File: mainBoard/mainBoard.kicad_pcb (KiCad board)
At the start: 4 copper layers, 50 x 60 mm, 43 parts, among them J1 Conn_01x04, J10 Conn_02x07_Odd_Even, J2 Conn_01x04, J4 Conn_01x01, J5 Conn_01x01, J6 Conn_01x07, J7 Conn_01x07, J8 Conn_01x02, J9 Conn_01x08, U1 MAX15062A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

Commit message: Popisky
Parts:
- renumbered J4 to M1, J5 to M2
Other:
- board text added: "+"
- board text added: "-"
- board text added: "BAT_SENS"
- board text added: "ENC_POT"
- board text added: "G"
- board text added: "M1"
- board text added: "M2"
- board text added: "NRST"
- board text added: "PROUD"
- board text added: "R"
- board text added: "RST"
- board text added: "RX"
- board text added: "SWCLK"
- board text added: "SWDIO"
- board text added: "T"
- board text added: "TX"
- board text added: "VREF"

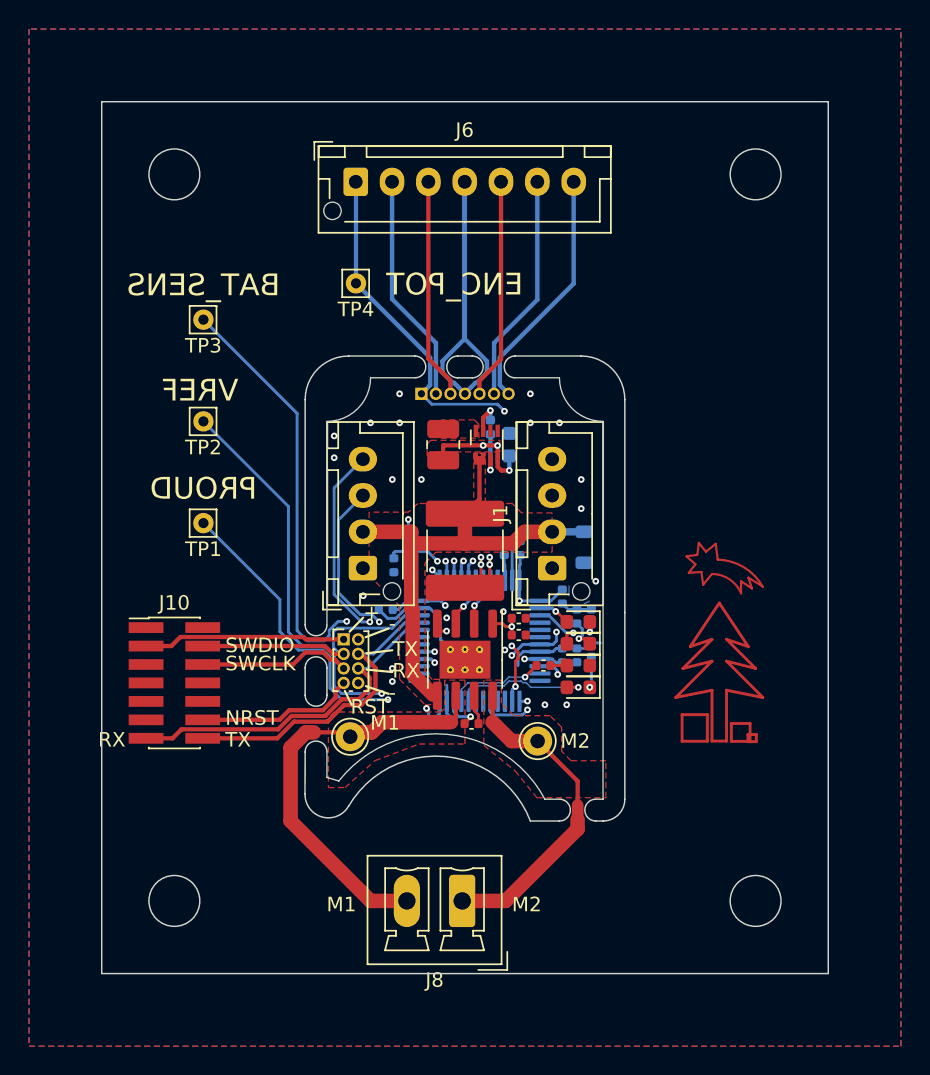
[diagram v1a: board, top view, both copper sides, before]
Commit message: Zvetšení test pointů
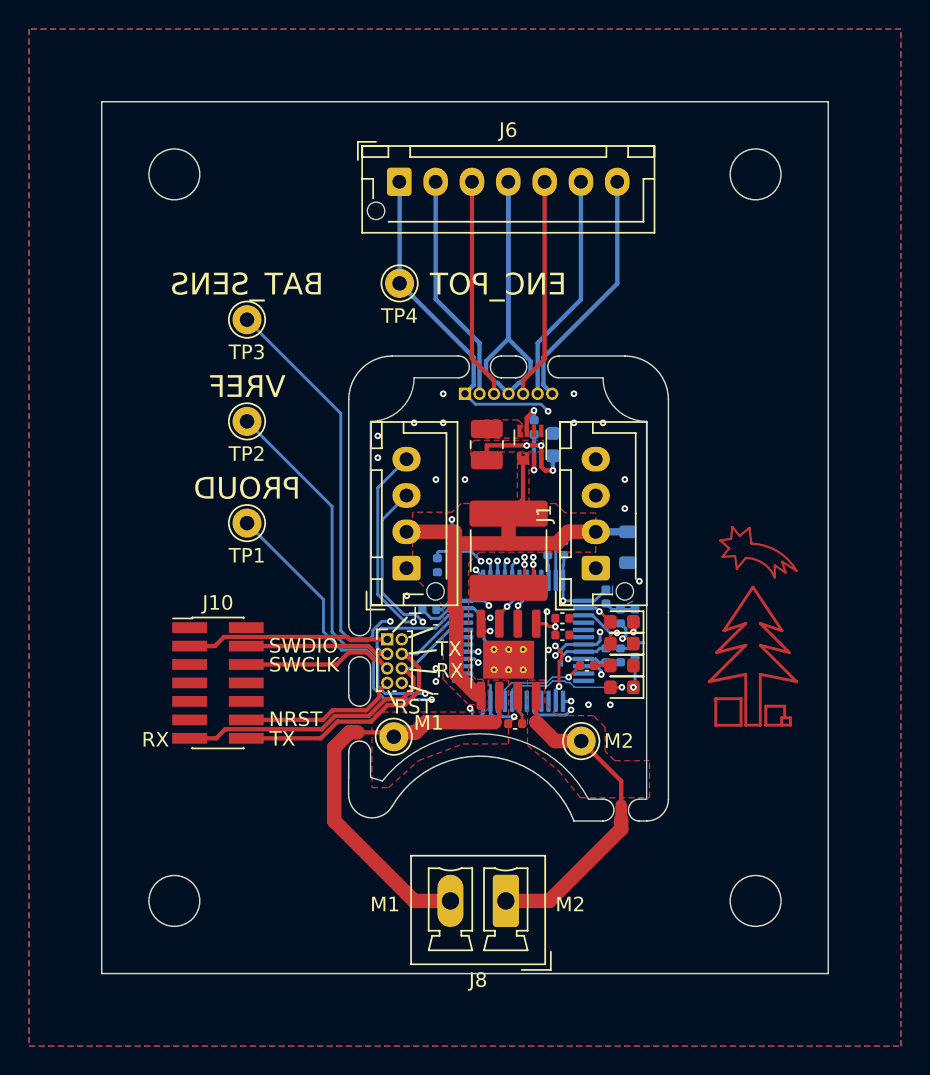
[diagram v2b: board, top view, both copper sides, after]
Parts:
- TP1, TP2, TP3, TP4: footprint Connector_Pin:Pin_D0.7mm_L6.5mm_W1.8mm_FlatFork -> Connector_Pin:Pin_D1.0mm_L10.0mm
- moved C1 3.00 mm to (148.1, 96.9)
- moved C10 3.00 mm to (159.7, 103.1)
- moved C11 3.00 mm to (153.4, 107.8)
- moved C12 3.00 mm to (160.7, 103.1)
- moved C13 3.00 mm to (155.7, 95.7)
- moved C14 3.00 mm to (153.0, 95.9)
- moved C15 3.00 mm to (156.7, 101.7)
- moved C2 3.00 mm to (161.2, 95.7)
- moved C3 3.00 mm to (154.8, 87.4)
- moved C4 3.00 mm to (156.1, 88.6)
- moved C5 3.00 mm to (149.6, 107.8)
- moved C6 3.00 mm to (147.6, 100.0)
- moved C7 3.00 mm to (159.7, 99.0)
- moved C8 3.00 mm to (151.5, 107.8)
- moved C9 3.00 mm to (156.8, 95.7)
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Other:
- outline, holes or cut-outs redrawn

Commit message: Hrádky s poligony
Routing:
- net GND: track 54.4 -> 76.8 mm
- net VCC: track 35.2 -> 36.2 mm
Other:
- board text added: "CLK"
- board text added: "E.TYP"
- board text added: "MISO"
- board text added: "MOSI"
- board text added: "POT"

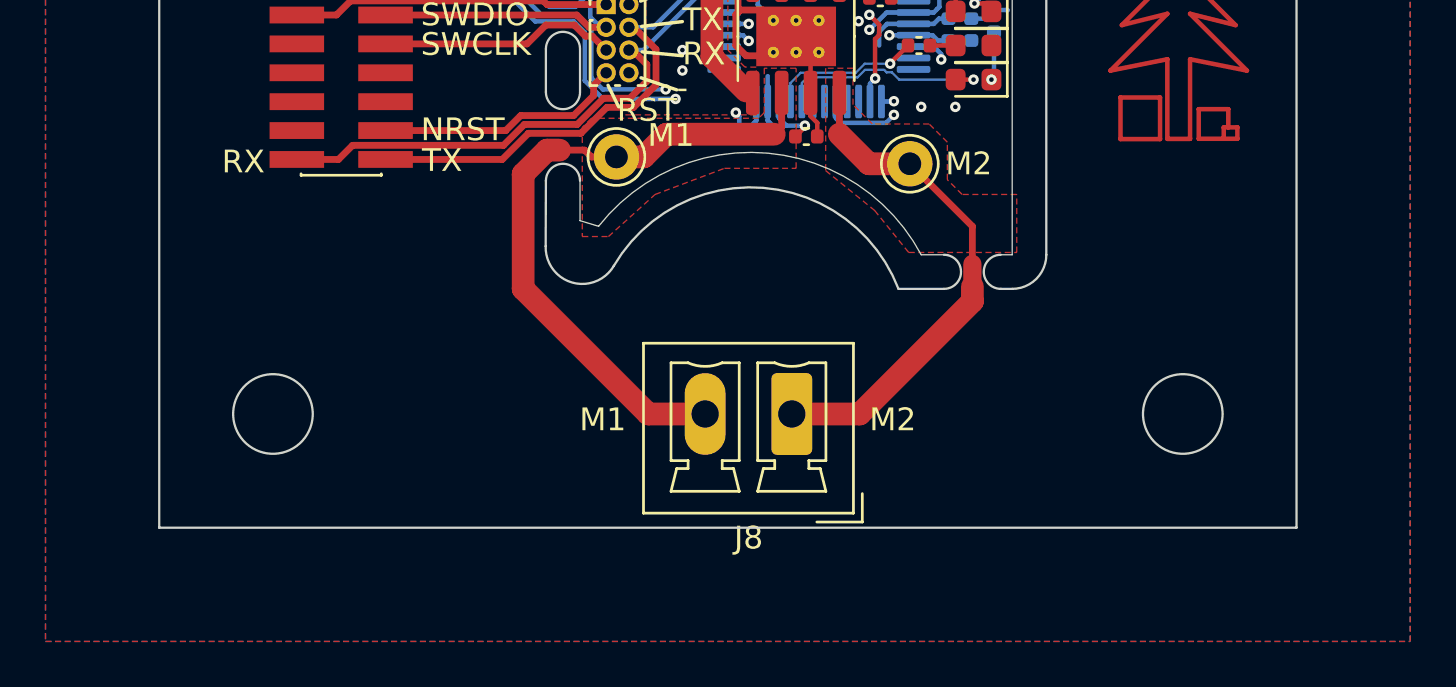
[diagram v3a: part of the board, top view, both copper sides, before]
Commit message: JST-XH na externí motorový konektor
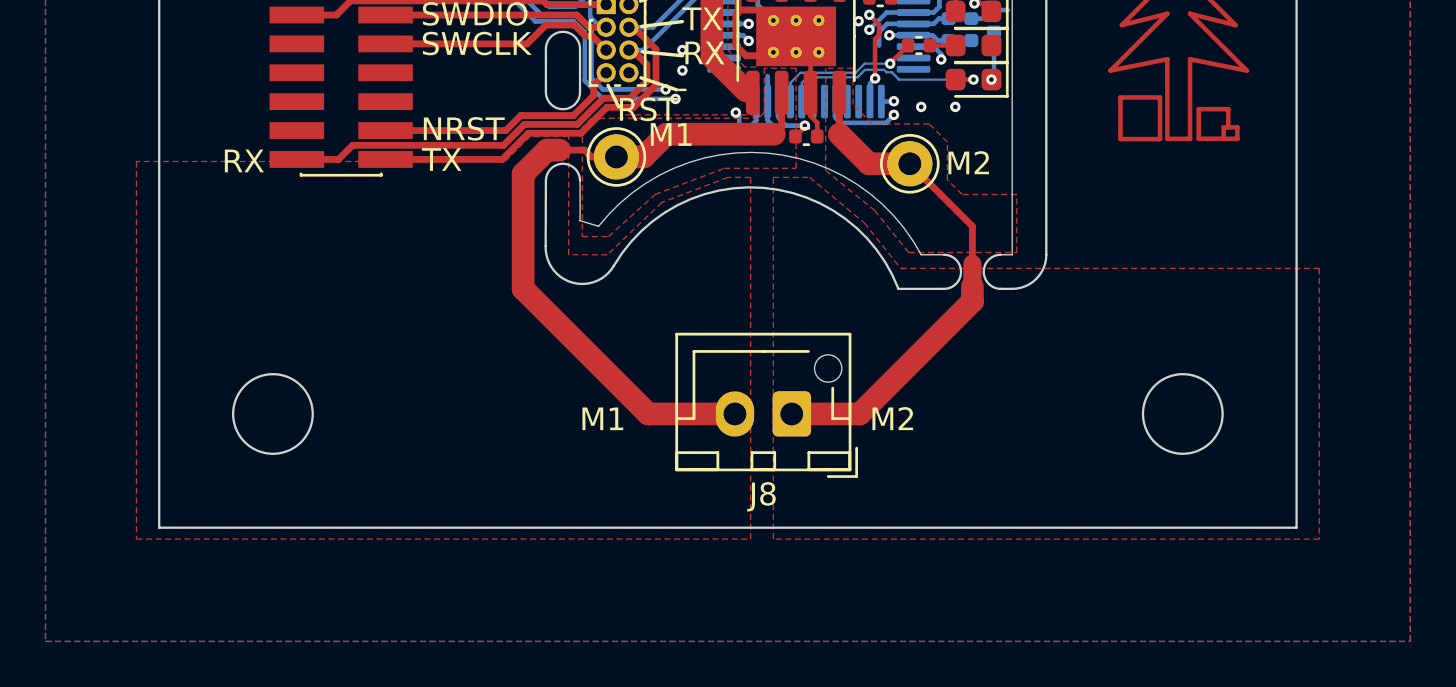
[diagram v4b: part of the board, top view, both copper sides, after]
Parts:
- J8: footprint Connector_Phoenix_MC:PhoenixContact_MCV_1,5_2-G-3.81_1x02_P3.81mm_Vertical -> Connector_JST:JST_XH_B2B-XH-AM_1x02_P2.50mm_Vertical
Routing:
- net Net-(J8-Pin_2): track 29.3 -> 30.6 mm

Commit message: Moc kondíků
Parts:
- added C16: 2u2, Capacitor_SMD:C_0805_2012Metric, F.Cu at (153.0, 92.5)
- added C17: 2u2, Capacitor_SMD:C_0805_2012Metric, F.Cu at (155.1, 92.5)
- added C18: 2u2, Capacitor_SMD:C_0805_2012Metric, F.Cu at (150.9, 96.0)
- added C19: 2u2, Capacitor_SMD:C_0805_2012Metric, F.Cu at (153.0, 96.0)
- added C20: 2u2, Capacitor_SMD:C_0805_2012Metric, F.Cu at (155.1, 96.0)
- added C22: 2u2, Capacitor_SMD:C_0805_2012Metric, F.Cu at (148.5, 102.3)
- added C23: 2u2, Capacitor_SMD:C_0805_2012Metric, F.Cu at (148.5, 104.2)
- added C24: 2u2, Capacitor_SMD:C_0805_2012Metric, F.Cu at (148.5, 106.2)
- added C25: 2u2, Capacitor_SMD:C_0805_2012Metric, F.Cu at (151.7, 98.7)
- added C26: 2u2, Capacitor_SMD:C_0805_2012Metric, B.Cu at (147.6, 106.5)
- added C27: 2u2, Capacitor_SMD:C_0805_2012Metric, B.Cu at (147.6, 102.9)
- added C28: 2u2, Capacitor_SMD:C_0805_2012Metric, B.Cu at (148.6, 95.9)
- added C29: 2u2, Capacitor_SMD:C_0805_2012Metric, B.Cu at (148.6, 92.3)
- added C30: 2u2, Capacitor_SMD:C_0805_2012Metric, B.Cu at (148.6, 88.5)
- added C31: 2u2, Capacitor_SMD:C_0805_2012Metric, B.Cu at (156.8, 92.6)
- added C32: 2u2, Capacitor_SMD:C_0805_2012Metric, B.Cu at (161.2, 92.1)
- added C33: 2u2, Capacitor_SMD:C_0805_2012Metric, B.Cu at (150.7, 88.5)
- added C34: 2u2, Capacitor_SMD:C_0805_2012Metric, B.Cu at (152.7, 88.5)
- C14: value 22u -> 2u2; footprint Capacitor_SMD:C_2220_5650Metric -> Capacitor_SMD:C_0805_2012Metric
- C2: value 1u -> 2u2; footprint Inductor_SMD:L_0805_2012Metric -> Capacitor_SMD:C_0805_2012Metric
- C3: footprint Inductor_SMD:L_0402_1005Metric -> Capacitor_SMD:C_0402_1005Metric
- moved C14 3.97 mm to (150.9, 92.5), turned to 90 degrees
- moved C1 3.94 mm to (145.6, 100.0), turned to 0 degrees
- moved R1 1.10 mm to (150.2, 95.0)
- moved R2 1.10 mm to (150.2, 96.9)
- moved J9 0.05 mm to (144.6, 102.0)
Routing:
- net VCC: track 36.2 -> 51.5 mm, vias 1 -> 4
- net GND: track 76.8 -> 82.6 mm
- net /CPU/UART.TX: track 29.8 -> 31.4 mm
- net /CPU/UART.RX: track 33.2 -> 34.3 mm
- net /CPU/ENC.ENC-TYP-DET: track 29.0 -> 29.8 mm
- net /CPU/ENC.MOSI: track 29.1 -> 28.4 mm
- net /CPU/RX-1: track 23.9 -> 24.6 mm, vias 0 -> 2
- net VDD: track 101.5 -> 102.2 mm
- net /CPU/TX-1: track 21.5 -> 20.9 mm
- net /CPU/SWCLK: track 23.5 -> 22.9 mm
- net /CPU/MEŘENÍ-NAPÁJENÍ: track 61.6 -> 61.0 mm
- added copper zone on In1.Cu, net GND
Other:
- board text removed: "RST"

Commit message: GNDDETECT
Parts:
- removed C34: 2u2, Capacitor_SMD:C_0805_2012Metric
- added C21: 2u2, Capacitor_SMD:C_0805_2012Metric, B.Cu at (152.7, 88.5)
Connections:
- J10 pad 11: unconnected-(J10-Pin_11-Pad11) -> GND

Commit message: 16x20
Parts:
- removed C19, C20, C21, C22, C23, C24, C25, C26, C27, C28, C29, C30, C31, C32, C33: 2u2, Capacitor_SMD:C_0805_2012Metric
- removed J9: Conn_01x08, Connector_PinHeader_1.00mm:PinHeader_2x04_P1.00mm_Vertical
- added J3: Conn_01x03, Connector_PinHeader_1.00mm:PinHeader_1x03_P1.00mm_Vertical, F.Cu at (145.6, 101.0)
- C10, C6, C7, C8, C9: footprint Capacitor_SMD:C_0402_1005Metric -> Capacitor_SMD:C_0201_0603Metric
- C11, R6: moved to B.Cu
- C14: value 2u2 -> 10u; moved to B.Cu
- C16, C17, C18: value 2u2 -> 10u
- C5, R5: moved to F.Cu
- J1, J2: footprint Connector_JST:JST_XH_B4B-XH-AM_1x04_P2.50mm_Vertical -> Connector_JST:JST_PH_B4B-PH-K_1x04_P2.00mm_Vertical
- J6: footprint Connector_JST:JST_XH_B7B-XH-AM_1x07_P2.50mm_Vertical -> Connector_JST:JST_PH_B7B-PH-K_1x07_P2.00mm_Vertical
- J7: footprint Connector_PinHeader_1.00mm:PinHeader_1x07_P1.00mm_Vertical -> Connector_PinHeader_1.27mm:PinHeader_1x07_P1.27mm_Vertical
- moved D4 15.1 mm to (159.1, 88.8), turned to 0 degrees
- moved R6 15.0 mm to (159.1, 88.8)
- moved C17 13.5 mm to (148.5, 104.3), turned to 180 degrees
- moved J1 12.2 mm to (146.8, 98.0)
- moved J2 12.1 mm to (158.0, 98.0)
- moved C8 11.7 mm to (155.2, 96.7), turned to 180 degrees
- moved C6 11.0 mm to (158.6, 99.4), turned to 0 degrees
- moved C16 10.7 mm to (148.5, 102.2), turned to 180 degrees
- moved C7 10.5 mm to (153.7, 107.7), turned to 0 degrees
- moved C9 10.4 mm to (147.2, 99.7), turned to -90 degrees
- moved C14 10.2 mm to (160.1, 97.0), turned to -90 degrees
- moved C1 9.41 mm to (150.2, 91.8), turned to 90 degrees
- moved C2 8.10 mm to (153.3, 93.7), turned to 0 degrees
- moved C3 7.77 mm to (154.2, 95.2), turned to 0 degrees
- moved C11 7.35 mm to (146.4, 105.5), turned to 180 degrees
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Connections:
- D4 pad 1: GND -> Net-(D4-K)
- D4 pad 2: Net-(D4-A) -> /CPU/LED.Y
- R6 pad 1: /CPU/LED.Y -> Net-(D4-K)
- R6 pad 2: Net-(D4-A) -> GND
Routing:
- net VCC: track 51.5 -> 8.02 mm, vias 4 -> 5
- net Net-(J8-Pin_2): track 30.6 -> 6.43 mm
- net /CPU/LED.Y: track 6.67 -> 26.9 mm, vias 1 -> 3
- net GND: track 82.6 -> 62.6 mm, vias 23 -> 5
- net Net-(J8-Pin_1): track 22.6 -> 3.10 mm
- net /CPU/ENC.MISO: track 45.0 -> 28.1 mm
- net VDD: track 102.2 -> 91.7 mm, vias 7 -> 10
- net /CPU/MEŘENÍ-NAPÁJENÍ: track 61.0 -> 53.4 mm, vias 5 -> 3
- net /CPU/UART.RX: track 34.3 -> 26.7 mm, vias 2 -> 1
- net /CPU/UART.TX: track 31.4 -> 23.9 mm, vias 2 -> 1
- net /CPU/SWCLK: track 22.9 -> 18.7 mm
- net Net-(C11-Pad1): track 2.66 -> 5.49 mm, vias 1 -> 0
- net /CPU/SWDIO: track 18.1 -> 15.5 mm
- net /CPU/DRV.VREF: track 44.0 -> 41.4 mm, vias 4 -> 3
- net Net-(U1-LX): track 0.00 -> 2.10 mm
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- added copper zone on B.Cu, net VCC
- added copper zone on B.Cu, net VDD
- removed copper zone on F.Cu, net Net-(U1-LX)
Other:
- outline, holes or cut-outs redrawn
- board text removed: "G"
- board text removed: "R"
- board text removed: "T"

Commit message: Otočitelnost
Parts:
- R5: moved to B.Cu
- R6: moved to F.Cu
- moved D4 14.5 mm to (156.9, 103.2), turned to -90 degrees
- moved R6 12.4 mm to (156.7, 101.0), turned to 180 degrees
- moved R5 2.77 mm to (160.1, 102.9)
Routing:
- net /CPU/LED.Y: track 26.9 -> 9.78 mm, vias 3 -> 2
- net /CPU/LED.B: track 4.84 -> 5.49 mm
- net Net-(D3-K): track 1.31 -> 1.62 mm, vias 0 -> 1
- net Net-(D4-K): track 1.69 -> 1.52 mm, vias 1 -> 0
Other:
- outline, holes or cut-outs redrawn
